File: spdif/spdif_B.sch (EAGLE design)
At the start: 66 parts, among them T1 DA101MC, T2 DA101MC, U1 NC7SZ175, U2 FIN1001, U3 FIN1002, U4 NC7SZ175, U5 NC7SZ175, U6 FIN1002

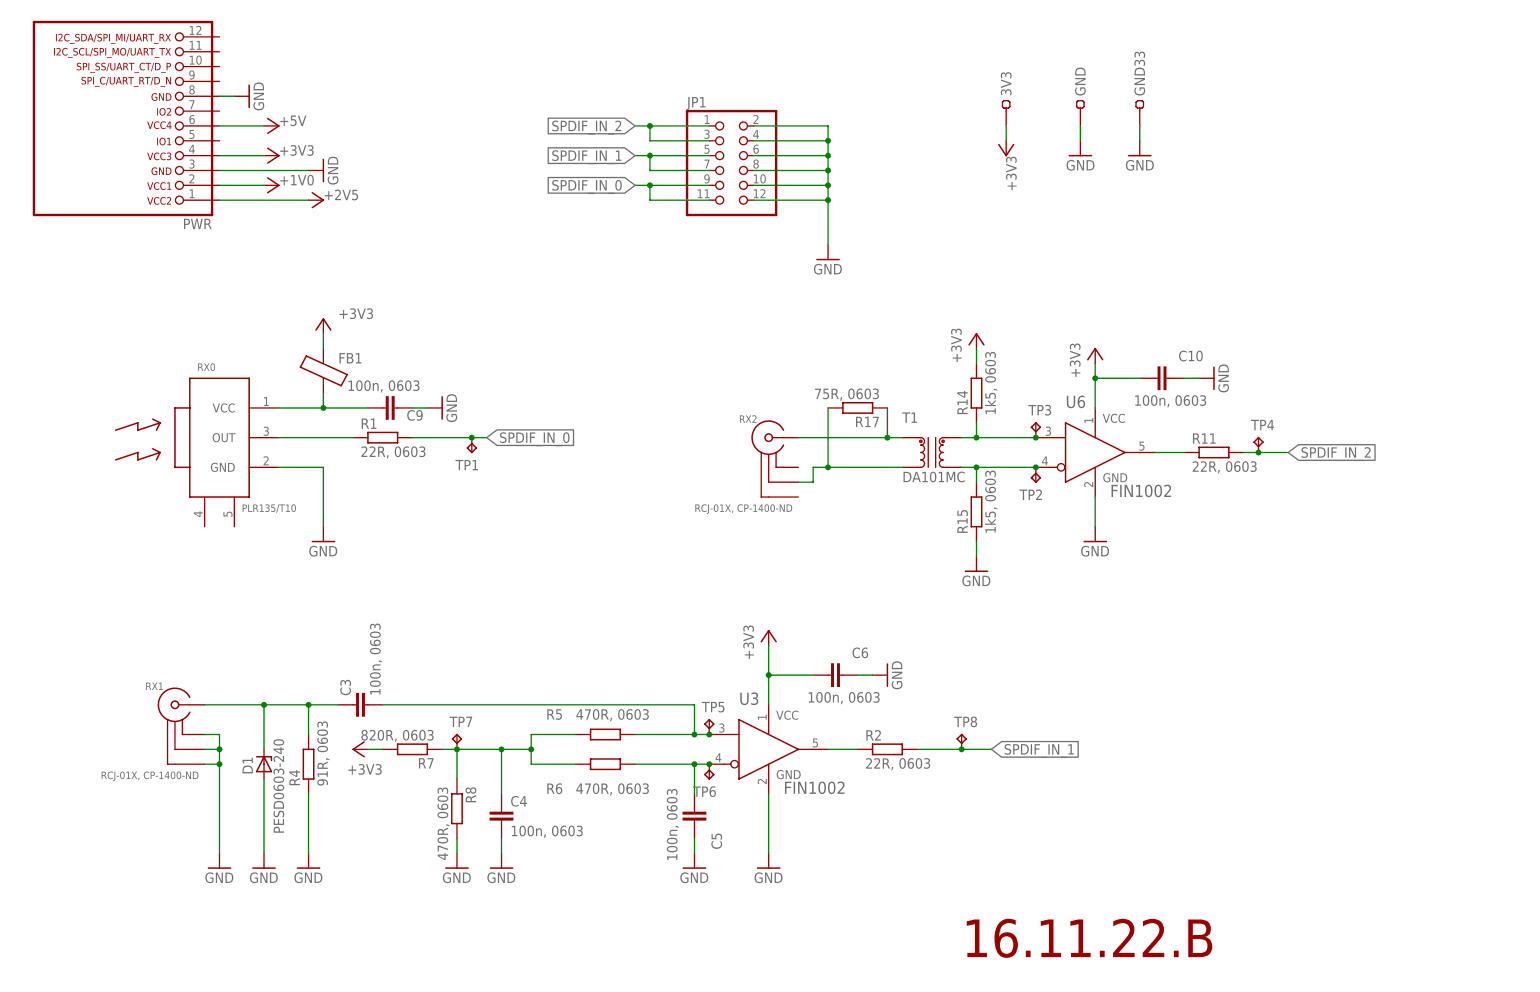
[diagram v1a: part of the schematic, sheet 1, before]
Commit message: spdif: B variant PCB finished
Signed-off-by: malo <pavol.malosek@gmail.com>
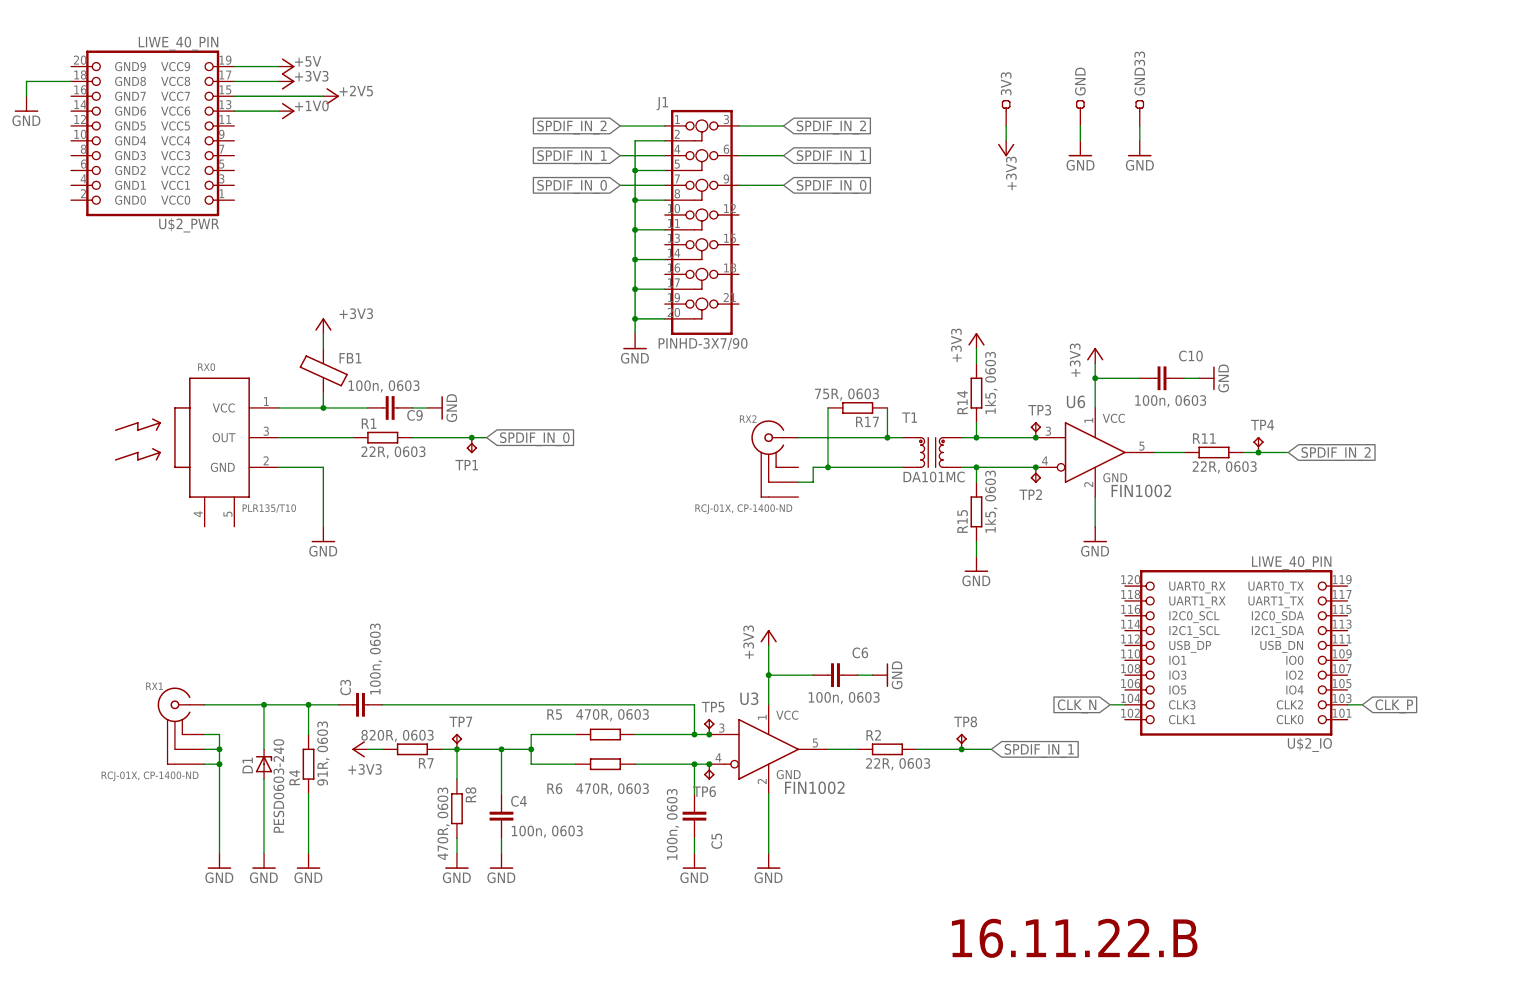
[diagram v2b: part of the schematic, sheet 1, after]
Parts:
- removed JP1, JP2: (no value), 25pinhead:PINHD-2X6/90
- removed PWR: (no value), 25cmsquare:LIWE_12_PIN_PWR8X8_COMPAT
- added C14: 100n, 0603, rcl:C-EUC0603
- added CLK0, CLK1, CLK2, TP_CLK: TPB1,27, testpad:TPB1,27
- added J1, J2: PINHD-3X7/90, 25pinhead:PINHD-3X7/90
- added R3: , 0603, rcl:R-EU_R0603
- added U$2: LIWE_40_PIN, 25cmsquare:LIWE_40_PIN
- added U7: FIN1002, 25cmsquare:FIN1002
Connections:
- new net CLK_N: U$2_IO.CLK3, U7.RIN-
- new net CLK_P: U$2_IO.CLK2, U7.RIN+
- new net N$10: R3.1, TP_CLK.TP
- new net N$9: R3.2, U7.ROUT
- net +1V0: now also U$2_PWR.VCC6; no longer PWR.2
- net +2V5: now also U$2_PWR.VCC7; no longer PWR.1
- net +3V3: now also C14.2, U$2_PWR.VCC8, U7.VCC; no longer PWR.4
- net +5V: now also U$2_PWR.VCC9; no longer PWR.6
- net CLK_0: now also CLK0.TP, J2.7, J2.9; no longer JP2.3
- net CLK_1: now also CLK1.TP, J2.13, J2.15; no longer JP2.7
- net CLK_2: now also CLK2.TP, J2.19, J2.21; no longer JP2.11
- net GND: now also C14.1, J1.11, J1.14, J1.17, J1.2, J1.20, J1.5, J1.8, J2.11, J2.14, J2.17, J2.2, J2.20, J2.5, J2.8, U$2_PWR.GND8, U7.GND; no longer JP1.10, JP1.12, JP1.2, JP1.4, JP1.6, JP1.8, JP2.10, JP2.12, JP2.2, JP2.4, JP2.6, JP2.8, PWR.3, PWR.8
- net SPDIF_IN_0: now also J1.7, J1.9; no longer JP1.11, JP1.9
- net SPDIF_IN_1: now also J1.4, J1.6; no longer JP1.5, JP1.7
- net SPDIF_IN_2: now also J1.1, J1.3; no longer JP1.1, JP1.3
- net SPDIF_OUT_0: now also J2.4, J2.6; no longer JP2.1
- net SPDIF_OUT_1: now also J2.10, J2.12; no longer JP2.5
- net SPDIF_OUT_2: now also J2.16, J2.18; no longer JP2.9

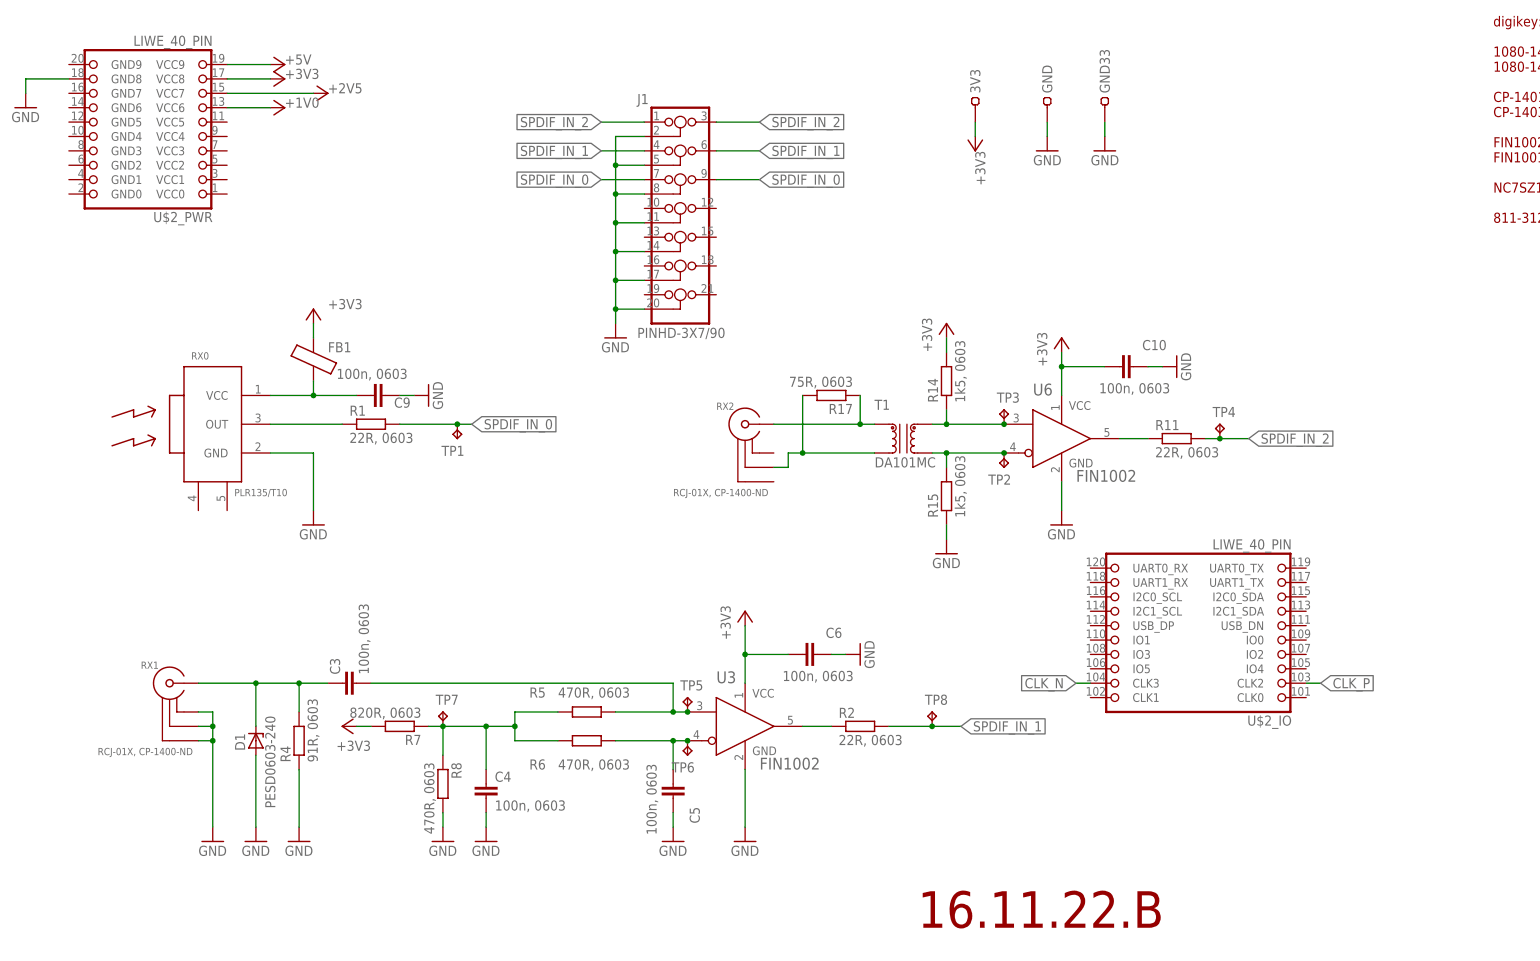
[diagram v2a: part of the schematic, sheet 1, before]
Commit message: spdif: added diff signaling for TX/RX 2
Signed-off-by: malo <pavol.malosek@gmail.com>
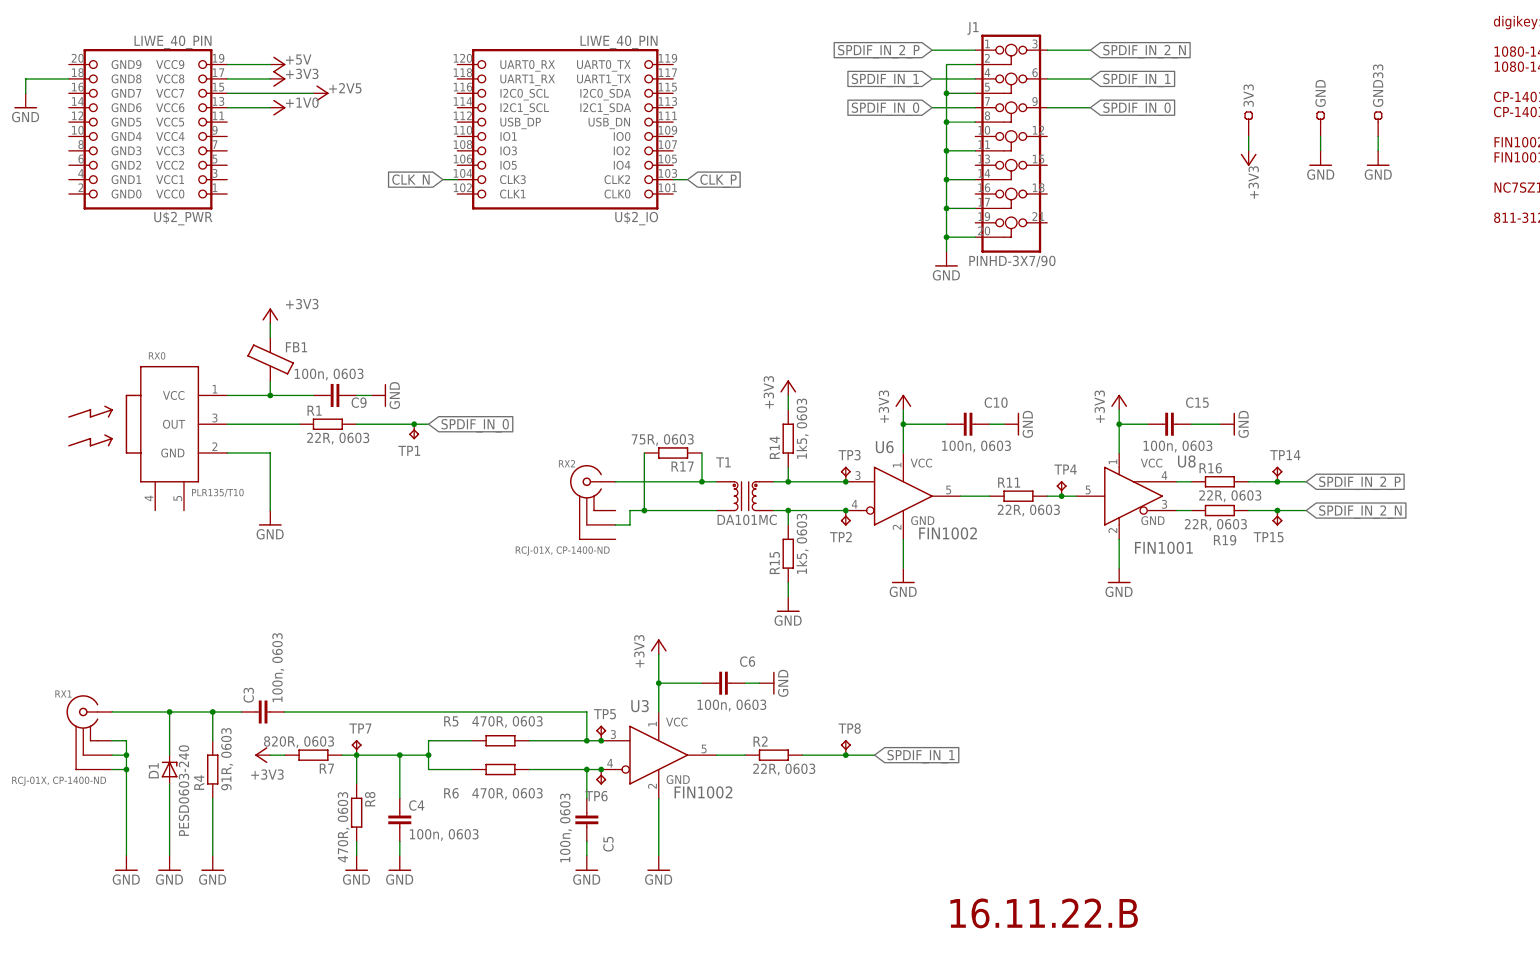
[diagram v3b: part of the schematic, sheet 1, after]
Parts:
- added C15, C16: 100n, 0603, rcl:C-EUC0603
- added R16, R19, R21, R22, R23, R24: 22R, 0603, rcl:R-EU_R0603
- added TP14, TP15: TPB1,27, testpad:TPB1,27
- added U8: FIN1001, 25cmsquare:FIN1001
- added U9: FIN1002, 25cmsquare:FIN1002
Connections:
- net N$7 renamed U6_OUT
- removed net SPDIF_IN_2: J1.1, J1.3, R11.2, TP4.TP
- removed net SPDIF_OUT_2: J2.16, J2.18, U1.D
- new net CLK_IN: R21.2, R22.2, R23.2, R3.1, TP_CLK.TP
- new net N$1: R11.2, TP4.TP, U8.RIN
- new net N$2: R16.1, U8.ROUT+
- new net N$7: R19.1, U8.ROUT-
- new net N$8: R24.2, U9.ROUT
- new net SPDIF_IN_2_N: J1.3, R19.2, TP15.TP
- new net SPDIF_IN_2_P: J1.1, R16.2, TP14.TP
- new net SPDIF_OUT_2_N: J2.18, U9.RIN-
- new net SPDIF_OUT_2_P: J2.16, U9.RIN+
- net +3V3: now also C15.2, C16.2, U8.VCC, U9.VCC
- net CLK_0: now also R21.1
- net CLK_1: now also R22.1
- net CLK_2: now also R23.1
- net GND: now also C15.1, C16.1, U8.GND, U9.GND
- net N$10: now also R24.1, U1.D; no longer R3.1, TP_CLK.TP
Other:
- moved on the sheet: 3V3, C1, C10, C11, C14, C3, C4, C5, C6, C9, CLK0, CLK2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
